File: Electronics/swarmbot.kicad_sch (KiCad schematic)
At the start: 6 parts, among them J1 12x2 JST, J2 12x2 JST, J7 8P8C

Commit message: made some changes
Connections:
- net Left Switch Lower: now also J2.21 (Pin_21); no longer J2.20 (Pin_20)
- net Left Switch Top: now also J1.21 (Pin_21); no longer J1.20 (Pin_20)
- net Right Switch Lower: now also J2.22 (Pin_22); no longer J2.21 (Pin_21)
- net Right Switch Top: now also J1.22 (Pin_22); no longer J1.21 (Pin_21)
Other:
- sheet Lower PCB ports: added none; removed Charging Pad
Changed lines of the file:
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@@
-    (stroke (width 0) (type default) (color 0 0 0 0))
-  )
-  (wire (pts (xy 183.515 31.75) (xy 189.23 31.75))
     (stroke (width 0) (type default) (color 0 0 0 0))
   )
@@
     (effects (font (size 1.27 1.27)) (justify left bottom))
   )
-  (label "Left Switch Top" (at 107.95 138.43 0)
-    (effects (font (size 1.27 1.27)) (justify left bottom))
-  )
-  (label "Right Switch Top" (at 107.95 140.97 0)
+  (label "Left Switch Top" (at 107.95 140.97 0)
+    (effects (font (size 1.27 1.27)) (justify left bottom))
+  )
+  (label "Right Switch Top" (at 107.95 143.51 0)
     (effects (font (size 1.27 1.27)) (justify left bottom))
   )
@@
     (effects (font (size 1.27 1.27)) (justify left bottom))
   )
-  (label "Left Switch Lower" (at 217.17 138.43 0)
-    (effects (font (size 1.27 1.27)) (justify left bottom))
-  )
-  (label "Right Switch Lower" (at 217.17 140.97 0)
+  (label "Left Switch Lower" (at 217.17 140.97 0)
+    (effects (font (size 1.27 1.27)) (justify left bottom))
+  )
+  (label "Right Switch Lower" (at 217.17 143.51 0)
     (effects (font (size 1.27 1.27)) (justify left bottom))
   )
@@
       (effects (font (size 1.27 1.27)) (justify left))
     )
-    (pin "Charging Pad" output (at 189.23 31.75 180)
-      (effects (font (size 1.27 1.27)) (justify left))
-    )

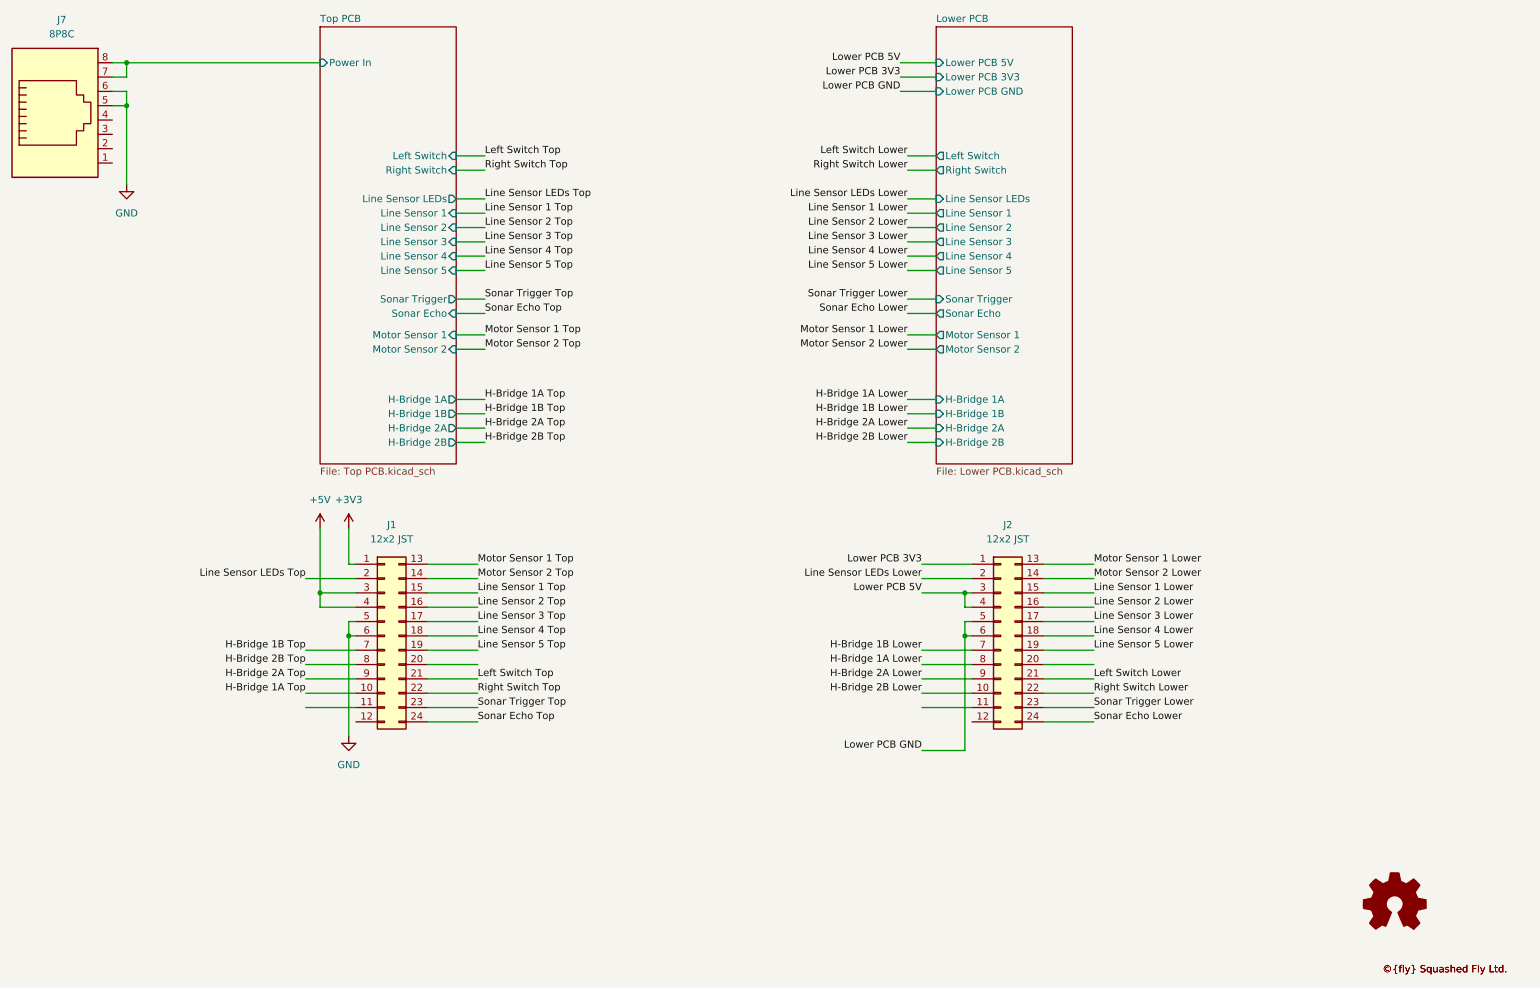
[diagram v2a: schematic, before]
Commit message: added bom
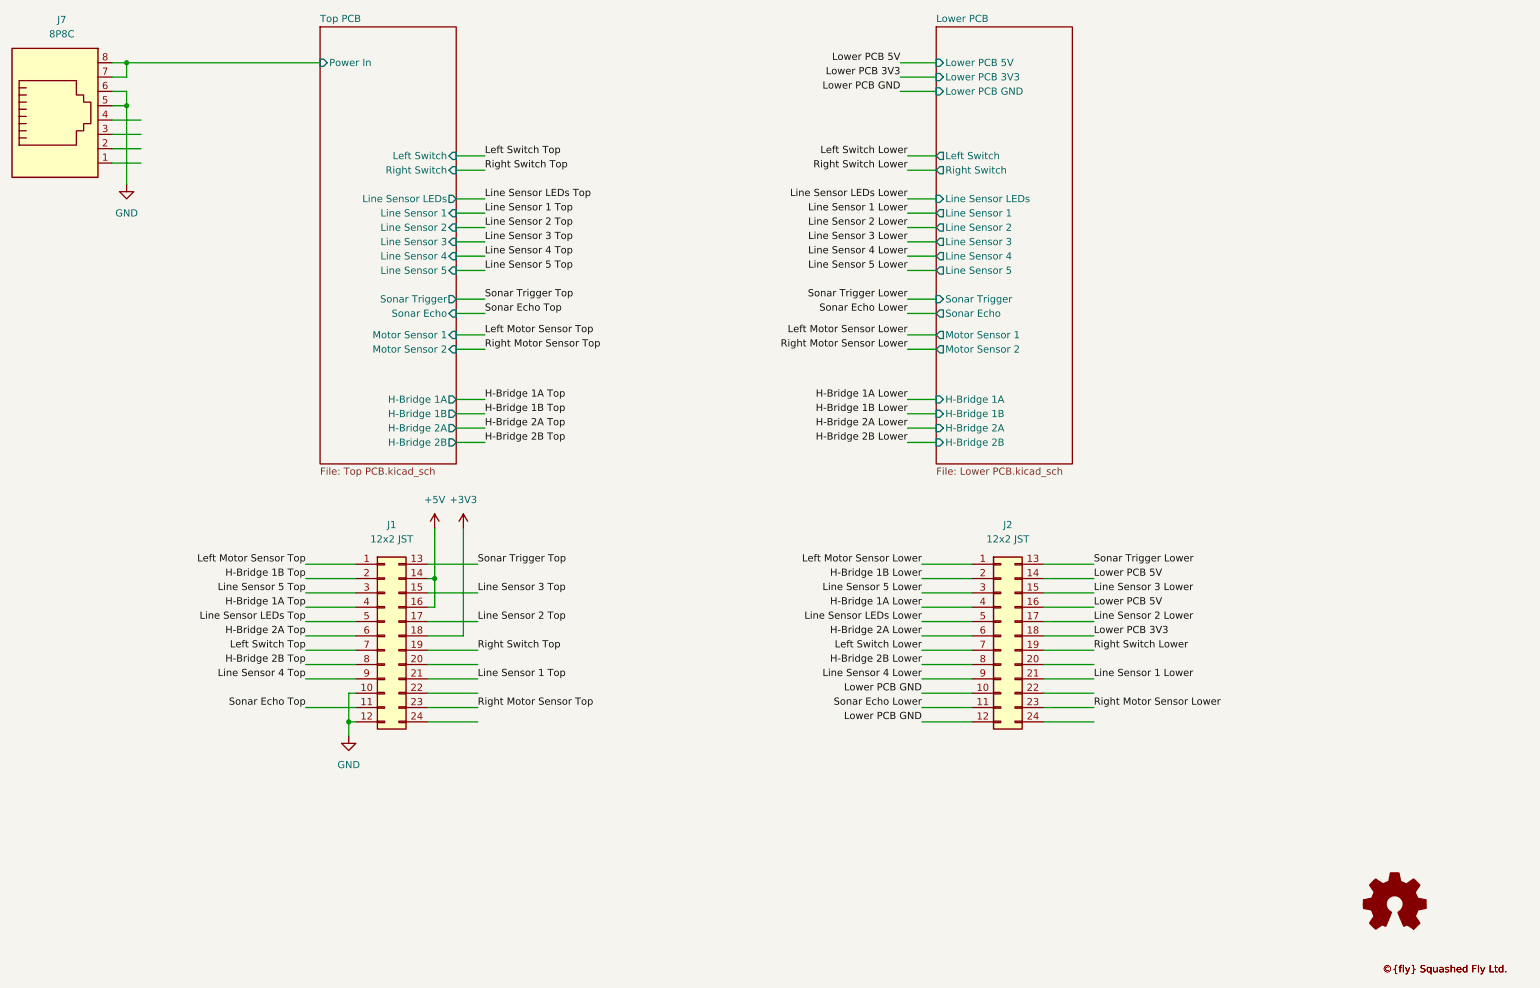
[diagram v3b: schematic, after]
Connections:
- net Motor Sensor 1 Lower is gone; now on net Sonar Trigger Lower: J2.13 (Pin_13)
- net Motor Sensor 1 Top is gone; now on net Sonar Trigger Top: J1.13 (Pin_13)
- net Motor Sensor 2 Lower is gone; now on net Lower PCB 5V: J2.14 (Pin_14)
- net Motor Sensor 2 Top is gone; now on net +5V: J1.14 (Pin_14)
- net +3V3: now also J1.18 (Pin_18); no longer J1.1 (Pin_1)
- net +5V: now also J1.16 (Pin_16); no longer J1.3 (Pin_3), J1.4 (Pin_4)
- net GND: now also J1.10 (Pin_10), J1.12 (Pin_12); no longer J1.5 (Pin_5), J1.6 (Pin_6)
- net H-Bridge 1A Lower: now also J2.4 (Pin_4); no longer J2.8 (Pin_8)
- net H-Bridge 1A Top: now also J1.4 (Pin_4); no longer J1.10 (Pin_10)
- net H-Bridge 1B Lower: now also J2.2 (Pin_2); no longer J2.7 (Pin_7)
- net H-Bridge 1B Top: now also J1.2 (Pin_2); no longer J1.7 (Pin_7)
- net H-Bridge 2A Lower: now also J2.6 (Pin_6); no longer J2.9 (Pin_9)
- net H-Bridge 2A Top: now also J1.6 (Pin_6); no longer J1.9 (Pin_9)
- net H-Bridge 2B Lower: now also J2.8 (Pin_8); no longer J2.10 (Pin_10)
- net Left Switch Lower: now also J2.7 (Pin_7); no longer J2.21 (Pin_21)
- net Left Switch Top: now also J1.7 (Pin_7); no longer J1.21 (Pin_21)
- net Line Sensor 1 Lower: now also J2.21 (Pin_21); no longer J2.15 (Pin_15)
- net Line Sensor 1 Top: now also J1.21 (Pin_21); no longer J1.15 (Pin_15)
- net Line Sensor 2 Lower: now also J2.17 (Pin_17); no longer J2.16 (Pin_16)
- net Line Sensor 2 Top: now also J1.17 (Pin_17); no longer J1.16 (Pin_16)
- net Line Sensor 3 Lower: now also J2.15 (Pin_15); no longer J2.17 (Pin_17)
- net Line Sensor 3 Top: now also J1.15 (Pin_15); no longer J1.17 (Pin_17)
- net Line Sensor 4 Lower: now also J2.9 (Pin_9); no longer J2.18 (Pin_18)
- net Line Sensor 4 Top: now also J1.9 (Pin_9); no longer J1.18 (Pin_18)
- net Line Sensor 5 Lower: now also J2.3 (Pin_3); no longer J2.19 (Pin_19)
- net Line Sensor 5 Top: now also J1.3 (Pin_3); no longer J1.19 (Pin_19)
- net Line Sensor LEDs Lower: now also J2.5 (Pin_5); no longer J2.2 (Pin_2)
- net Line Sensor LEDs Top: now also J1.5 (Pin_5); no longer J1.2 (Pin_2)
- net Lower PCB 3V3: now also J2.18 (Pin_18); no longer J2.1 (Pin_1)
- net Lower PCB 5V: now also J2.16 (Pin_16); no longer J2.3 (Pin_3), J2.4 (Pin_4)
- net Lower PCB GND: now also J2.10 (Pin_10), J2.12 (Pin_12); no longer J2.5 (Pin_5), J2.6 (Pin_6)
- net Right Switch Lower: now also J2.19 (Pin_19); no longer J2.22 (Pin_22)
- net Right Switch Top: now also J1.19 (Pin_19); no longer J1.22 (Pin_22)
- net Sonar Echo Lower: now also J2.11 (Pin_11); no longer J2.24 (Pin_24)
- net Sonar Echo Top: now also J1.11 (Pin_11); no longer J1.24 (Pin_24)
- net Sonar Trigger Lower: no longer J2.23 (Pin_23)
- net Sonar Trigger Top: no longer J1.23 (Pin_23)
- new net Left Motor Sensor Lower: J2.1 (Pin_1)
- new net Left Motor Sensor Top: J1.1 (Pin_1)
- new net Right Motor Sensor Lower: J2.23 (Pin_23)
- new net Right Motor Sensor Top: J1.23 (Pin_23)

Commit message: del backups
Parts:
- renumbered J7 to J1, J1 to J2, J2 to J3

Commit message: yep
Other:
- moved on the sheet: J1

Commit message: some changes were made
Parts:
- removed J1: 8P8C, Connector_RJ:RJ45_Amphenol_54602-x08_Horizontal, symbol Connector:8P8C
- added Front1: Front, Connector_JST:JST_XH_B2B-XH-A_1x02_P2.50mm_Vertical, symbol Connector_Generic:Conn_01x02
- added J1: Top, Connector_JST:JST_XH_B2B-XH-A_1x02_P2.50mm_Vertical, symbol Connector_Generic:Conn_01x02
- J2, J3: value 12x2 JST -> 12x2 IDC; footprint Connector_JST:JST_PUD_B24B-PUDSS_2x12_P2.00mm_Vertical -> Connector_IDC:IDC-Header_2x12_P2.54mm_Vertical; Farnell 2320532 -> (none)
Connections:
- net +3V3: now also J2.23 (Pin_23); no longer J2.18 (Pin_18)
- net +5V: now also J2.21 (Pin_21); no longer J2.14 (Pin_14), J2.16 (Pin_16)
- net GND: now also J2.1 (Pin_1), J2.19 (Pin_19), Front1.2 (Pin_2), J1.2 (Pin_2); no longer J2.10 (Pin_10), J2.12 (Pin_12)
- net H-Bridge 1A Lower: now also J3.5 (Pin_5); no longer J3.4 (Pin_4)
- net H-Bridge 1A Top: now also J2.5 (Pin_5); no longer J2.4 (Pin_4)
- net H-Bridge 1B Lower: now also J3.3 (Pin_3); no longer J3.2 (Pin_2)
- net H-Bridge 1B Top: now also J2.3 (Pin_3); no longer J2.2 (Pin_2)
- net H-Bridge 2A Lower: now also J3.7 (Pin_7); no longer J3.6 (Pin_6)
- net H-Bridge 2A Top: now also J2.7 (Pin_7); no longer J2.6 (Pin_6)
- net H-Bridge 2B Lower: now also J3.9 (Pin_9); no longer J3.8 (Pin_8)
- net H-Bridge 2B Top: now also J2.9 (Pin_9); no longer J2.8 (Pin_8)
- net Left Motor Sensor Lower: now also J3.2 (Pin_2); no longer J3.1 (Pin_1)
- net Left Motor Sensor Top: now also J2.2 (Pin_2); no longer J2.1 (Pin_1)
- net Left Switch Lower: now also J3.8 (Pin_8); no longer J3.7 (Pin_7)
- net Left Switch Top: now also J2.8 (Pin_8); no longer J2.7 (Pin_7)
- net Line Sensor 1 Lower: now also J3.22 (Pin_22); no longer J3.21 (Pin_21)
- net Line Sensor 1 Top: now also J2.22 (Pin_22); no longer J2.21 (Pin_21)
- net Line Sensor 2 Lower: now also J3.18 (Pin_18); no longer J3.17 (Pin_17)
- net Line Sensor 2 Top: now also J2.18 (Pin_18); no longer J2.17 (Pin_17)
- net Line Sensor 3 Lower: now also J3.16 (Pin_16); no longer J3.15 (Pin_15)
- net Line Sensor 3 Top: now also J2.16 (Pin_16); no longer J2.15 (Pin_15)
- net Line Sensor 4 Lower: now also J3.10 (Pin_10); no longer J3.9 (Pin_9)
- net Line Sensor 4 Top: now also J2.10 (Pin_10); no longer J2.9 (Pin_9)
- net Line Sensor 5 Lower: now also J3.4 (Pin_4); no longer J3.3 (Pin_3)
- net Line Sensor 5 Top: now also J2.4 (Pin_4); no longer J2.3 (Pin_3)
- net Line Sensor LEDs Lower: now also J3.6 (Pin_6); no longer J3.5 (Pin_5)
- net Line Sensor LEDs Top: now also J2.6 (Pin_6); no longer J2.5 (Pin_5)
- net Lower PCB 3V3: now also J3.23 (Pin_23); no longer J3.18 (Pin_18)
- net Lower PCB 5V: now also J3.11 (Pin_11), J3.21 (Pin_21); no longer J3.14 (Pin_14), J3.16 (Pin_16)
- net Lower PCB GND: now also J3.1 (Pin_1), J3.19 (Pin_19); no longer J3.10 (Pin_10), J3.12 (Pin_12)
- net Right Motor Sensor Lower: now also J3.24 (Pin_24); no longer J3.23 (Pin_23)
- net Right Motor Sensor Top: now also J2.24 (Pin_24); no longer J2.23 (Pin_23)
- net Right Switch Lower: now also J3.20 (Pin_20); no longer J3.19 (Pin_19)
- net Right Switch Top: now also J2.20 (Pin_20); no longer J2.19 (Pin_19)
- net Sonar Echo Lower: now also J3.12 (Pin_12); no longer J3.11 (Pin_11)
- net Sonar Echo Top: now also J2.12 (Pin_12); no longer J2.11 (Pin_11)
- net Sonar Trigger Lower: now also J3.14 (Pin_14); no longer J3.13 (Pin_13)
- net Sonar Trigger Top: now also J2.14 (Pin_14); no longer J2.13 (Pin_13)
- net Top PCB/Power In: now also Front1.1 (Pin_1), J1.1 (Pin_1)
- new net Bottom PCB V: J2.17 (Pin_17)
- new net Bottom PCB Version: J3.17 (Pin_17)
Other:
- sheet Lower PCB ports: added Bottom PCB Version; removed none
- sheet Top PCB ports: added Bottom PCB V; removed none
- company: Philip McGaw -> Squashed Fly

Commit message: removed the backups
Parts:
- renumbered Front1 to J1, J1 to J2, J2 to J3, J3 to J4
